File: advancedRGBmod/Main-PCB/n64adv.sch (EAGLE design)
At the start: 110 parts, among them J5 2510-, U1 10CL010YE144, U2 ADV7125/ADV7123, U4 74LVC3G17, U5 S25FLXXXSO8-DUAL, U6 TLV70012DDC, U7 TLV70025DDC

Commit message: pcb update: add some additional pads for rst and ctrl io
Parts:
- added /RST_A, CTRL_A: SMD1, wirepad:SMD1
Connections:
- removed net N$25: R52.1, U1.DATA2/IO132, U5.WP#/IO2
- removed net N$74: R53.1, U1.DATA3/IO133, U5.HOLD#/IO3
- removed net N$78: U1.IO28, U8.TS
- new net N$56: R53.1, U5.HOLD#/IO3
- new net N$67: R52.1, U5.WP#/IO2
- net N$66: now also CTRL_A.P
- net N$70: now also /RST_A.P
- net VCCIO_CO: now also U8.TS
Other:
- note added: "PCB Design (c) 2017-2019 Peter Bartmann"
- moved on the sheet: CTRL

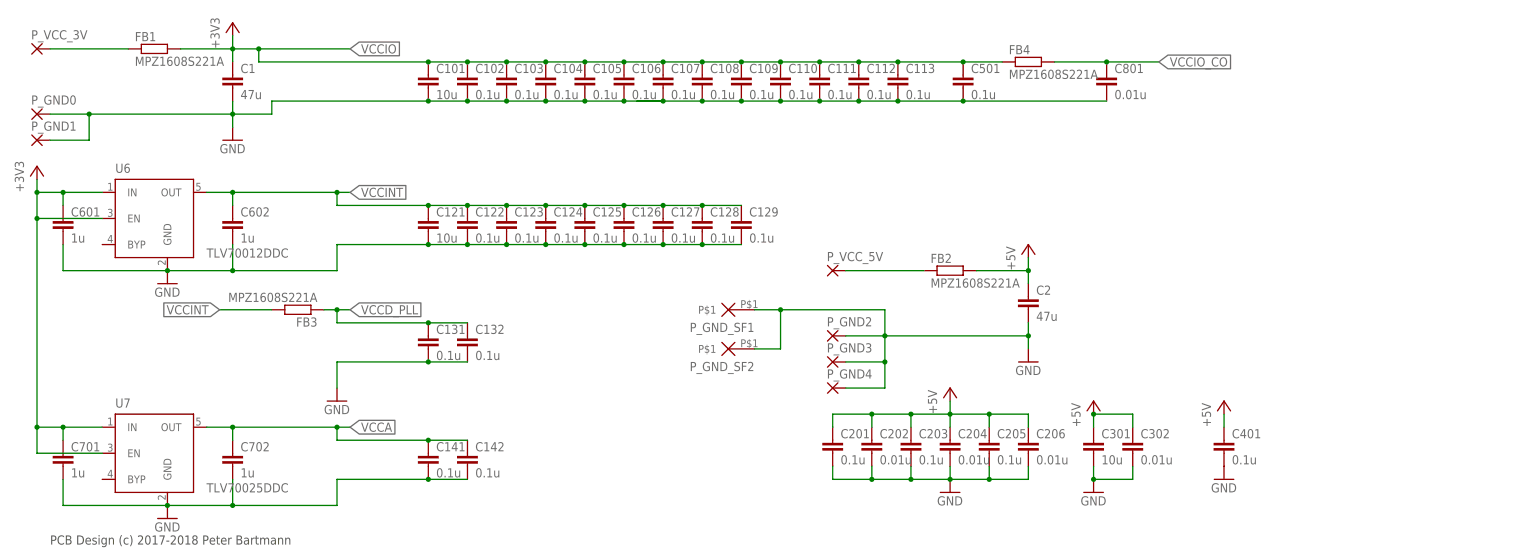
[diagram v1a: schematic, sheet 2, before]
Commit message: bank separation between digital video in and digital video outs using 2.5V LDO
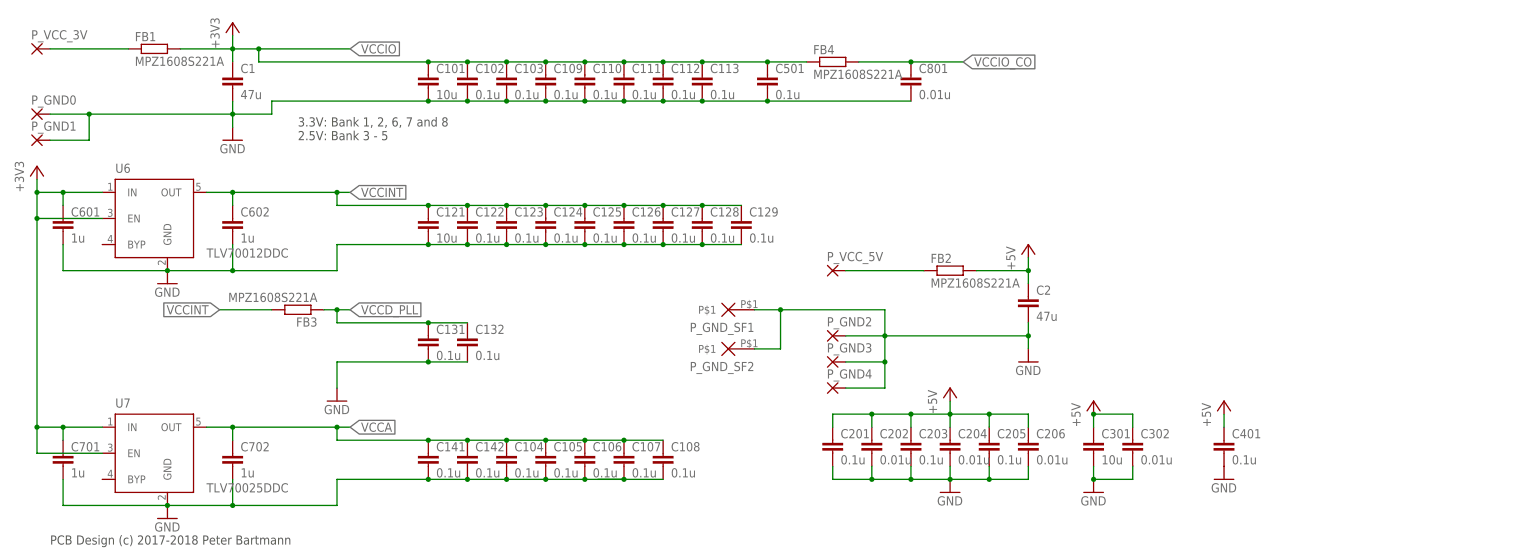
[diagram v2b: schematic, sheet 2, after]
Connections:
- net VCCA: now also C104.1, C105.1, C106.1, C107.1, C108.1, U1.VCCIO@3, U1.VCCIO@4, U1.VCCIO@5, U1.VCCIO@6, U1.VCCIO@7, U1.VREF/IO80
- net VCCIO: no longer C104.1, C105.1, C106.1, C107.1, C108.1, U1.VREF/IO80
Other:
- note added: "2.5V IOs"
- note added: "3.3V IOs"
- note added: "3.3V: Bank 1, 2, 6, 7 and 8 2.5V: Bank 3 - 5"
- note added: "3.3V: Bank 1, 2, 6, 7 and 8 2.5V: Bank 3 - 5 (VCCA)"
- moved on the sheet: C104, C105, C106, C107, C108, C109, C110, C111, C112, C113, C501, C801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

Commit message: update N64Adv board: - csync level selection by jumper - output IO bank powered by 5V rail (over a 3.3V ldo)
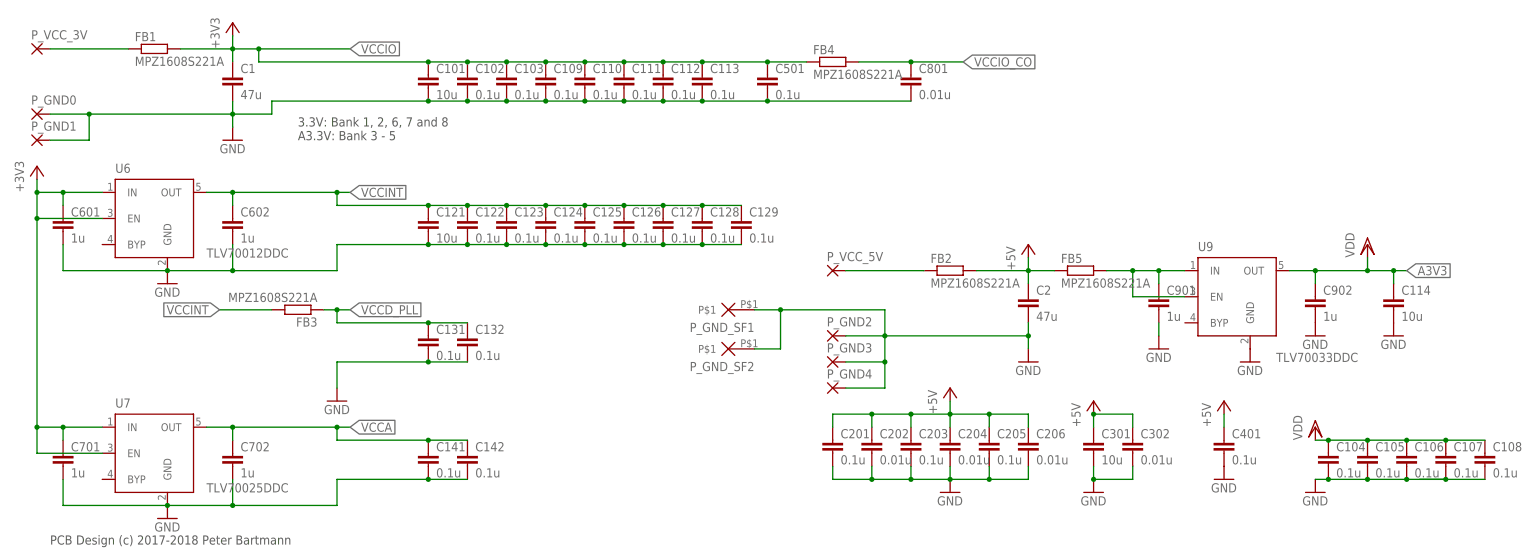
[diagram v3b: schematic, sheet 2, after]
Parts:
- removed /RST_A, CTRL_A: SMD1, wirepad:SMD1
- added C114: 10u, rcl:C-EUC0805
- added C901, C902: 1u, rcl:C-EUC0603
- added FB5: MPZ1608S221A, rcl:R-EU_R0603
- added J33: (no value), jumper:SJ
- added R34: 75, rcl:R-EU_R0603
- added U9: TLV70033DDC, v-reg-micrel:MIC5219XX
- /RST, CTRL: value (none) -> SMD1; device wirepad@1:SMD2 -> wirepad:SMD1
- C33: device rcl@1:C-EUC1210 -> rcl:C-EUC0805
- C34: device rcl:C-EUC1206 -> rcl:C-EUC0805
- R32: value 475 -> 6k19
- R33: value 75 -> 523
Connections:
- new net A3V3: C104.1, C105.1, C106.1, C107.1, C108.1, C114.1, C902.1, U1.VCCIO@3, U1.VCCIO@4, U1.VCCIO@5, U1.VCCIO@6, U1.VCCIO@7, U1.VREF/IO80, U9.OUT
- new net N$25: C901.1, FB5.2, U9.EN, U9.IN
- new net N$71: J33.1, R33.2
- net +5V: now also FB5.1
- net GND: now also C114.2, C901.2, C902.2, R33.1, U9.GND
- net N$1: now also J33.2
- net N$17: now also R34.1; no longer R33.1
- net N$21: now also R34.2; no longer R33.2
- net N$66: no longer CTRL_A.P
- net N$70: no longer /RST_A.P
- net VCCA: no longer C104.1, C105.1, C106.1, C107.1, C108.1, U1.VCCIO@3, U1.VCCIO@4, U1.VCCIO@5, U1.VCCIO@6, U1.VCCIO@7, U1.VREF/IO80
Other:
- note added: "3.3V: Bank 1, 2, 6, 7 and 8 A3.3V: Bank 3 - 5"
- note added: "A3.3V IOs"
- note added: "PCB Design (c) 2017-2020 Peter Bartmann"
- note removed: "2.5V IOs"
- note removed: "3.3V: Bank 1, 2, 6, 7 and 8 2.5V: Bank 3 - 5"
- note removed: "PCB Design (c) 2017-2019 Peter Bartmann"
- moved on the sheet: C104, C105, C106, C107, C108, R33
